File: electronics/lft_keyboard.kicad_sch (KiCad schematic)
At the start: 61 parts, among them J3 Conn_01x05_Female, J4 Conn_01x05_Male, SW1 SW_SPST, SW10 SW_SPST, SW11 SW_SPST, SW12 SW_SPST, SW13 SW_SPST, SW14 SW_SPST, SW15 SW_SPST, SW16 SW_SPST, SW17 SW_SPST, SW18 SW_SPST, SW19 SW_SPST, SW2 SW_SPST, SW20 SW_SPST, SW21 SW_SPST, SW22 SW_SPST, SW23 SW_SPST, SW24 SW_SPST, SW25 SW_SPST, SW26 SW_SPST, SW27 SW_SPST, SW28 SW_SPST, SW29 SW_SPST, SW3 SW_SPST, SW4 SW_SPST, SW5 SW_SPST, SW6 SW_SPST, SW7 SW_SPST, SW8 SW_SPST, SW9 SW_SPST, U2 PCA9675PW

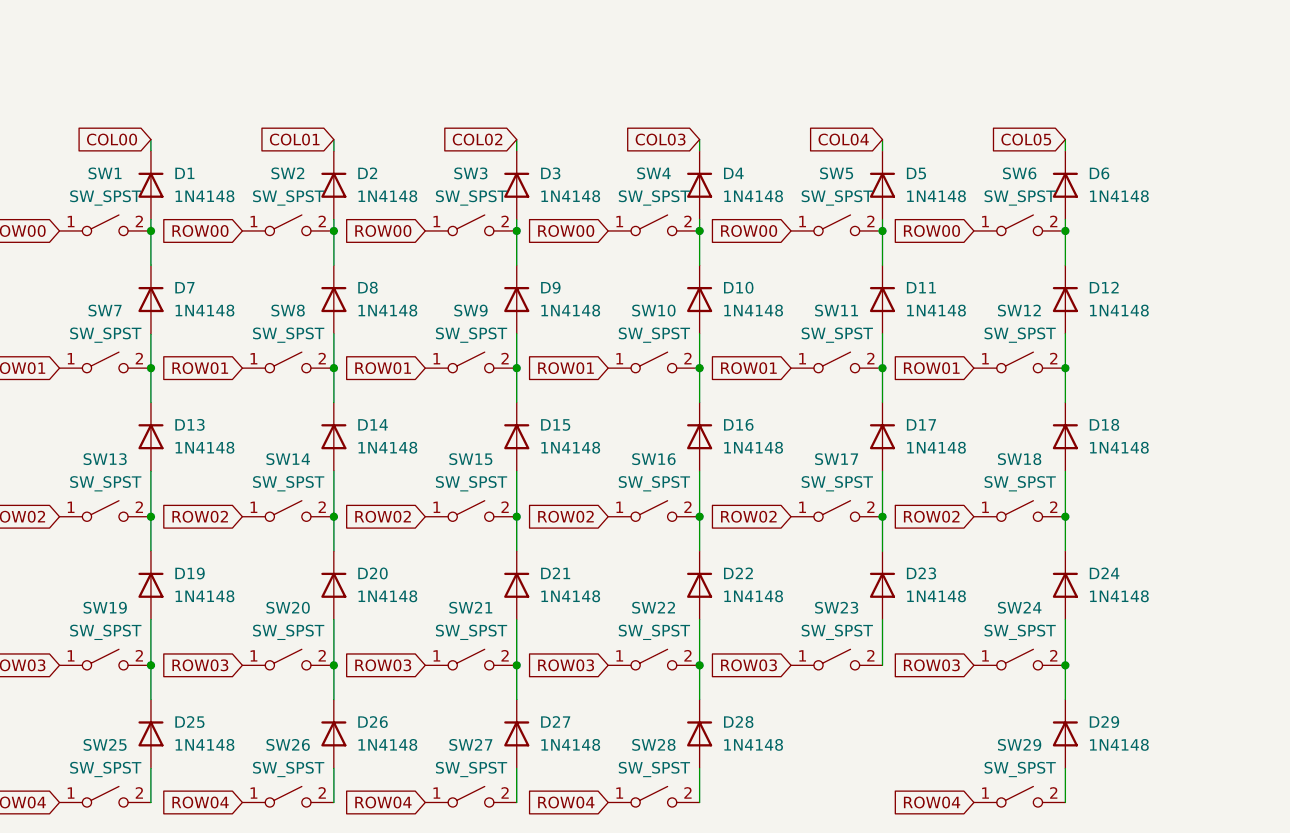
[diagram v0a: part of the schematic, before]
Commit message: update diode libraries
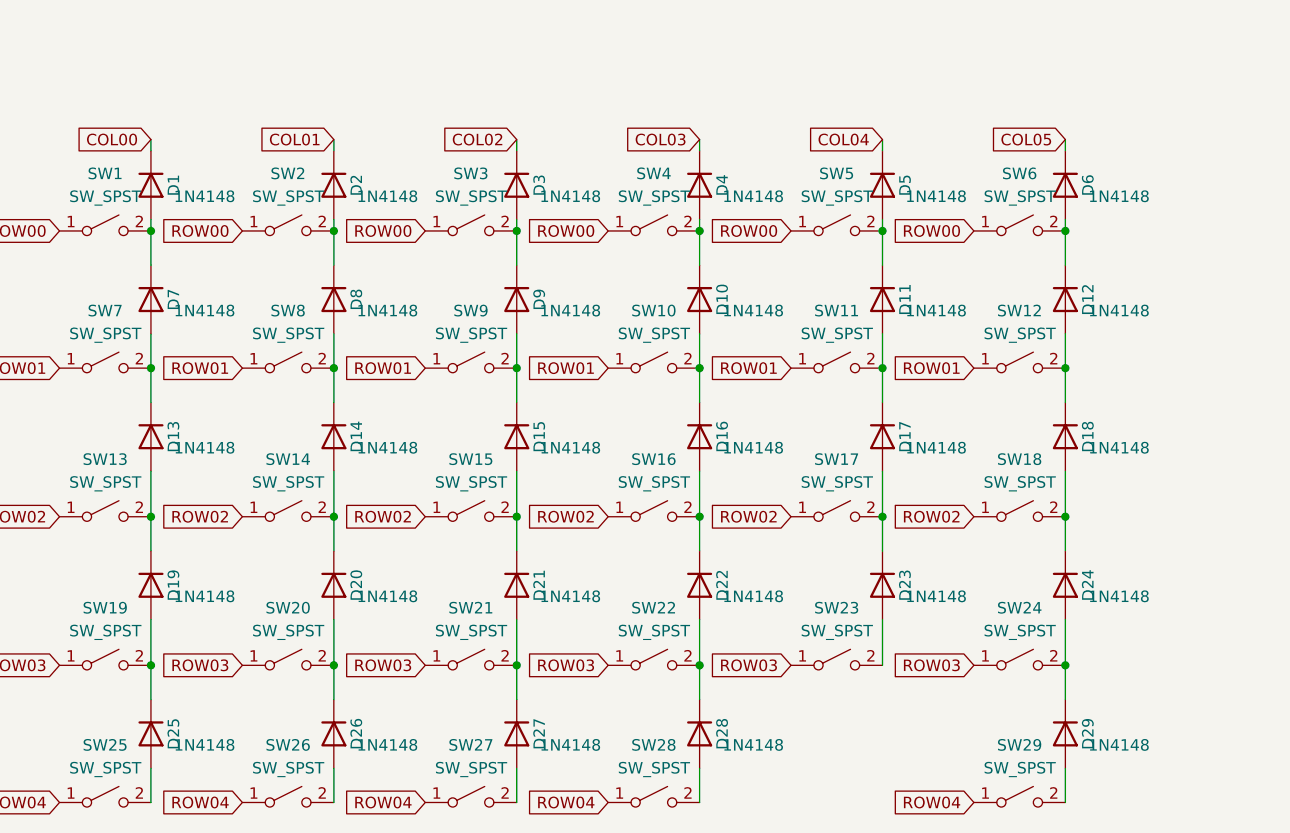
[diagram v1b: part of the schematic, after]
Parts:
- D1, D10, D11, D12, D13, D14, D15, D16, D17, D18, D19, D2, D20, D21, D22, D23, D24, D25, D26, D27, D28, D29, D3, D4, D5, D6, D7, D8, D9: footprint Diode_SMD:D_SOD-123 -> Diode_THT:D_DO-35_SOD27_P7.62mm_Horizontal; symbol Diode:1N4148W -> 1N4148:1N4148

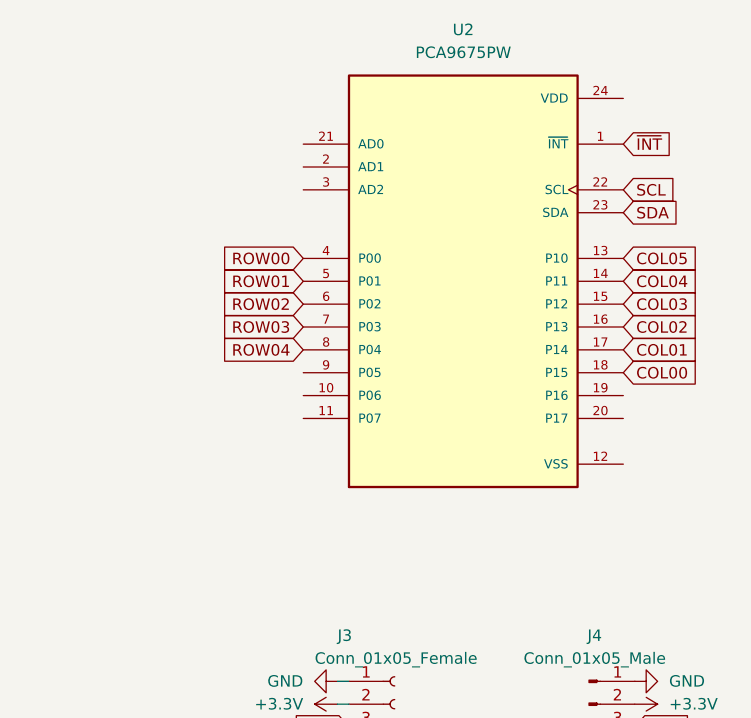
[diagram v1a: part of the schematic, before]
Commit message: add power and i2c addressing
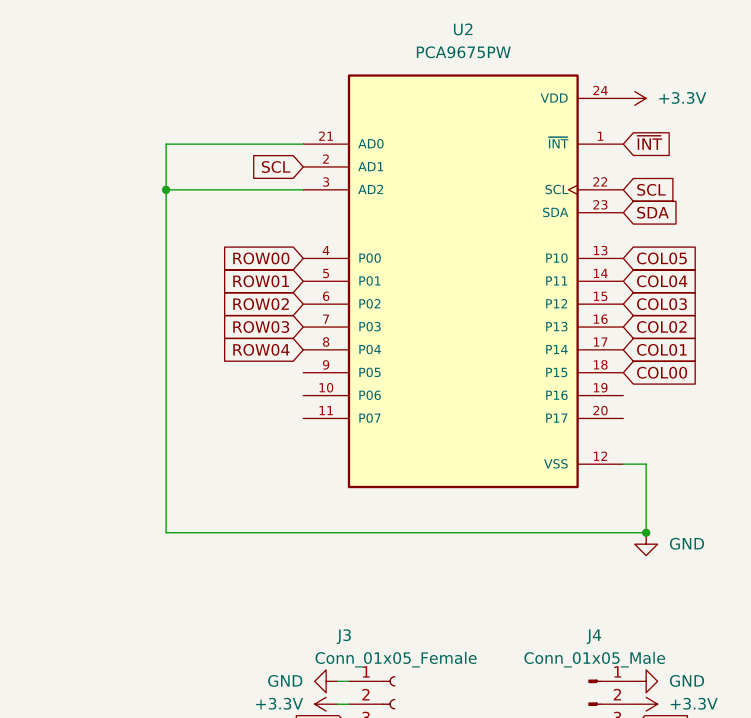
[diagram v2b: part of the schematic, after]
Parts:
- D1, D10, D11, D12, D13, D14, D15, D16, D17, D18, D19, D2, D20, D21, D22, D23, D24, D25, D26, D27, D28, D29, D3, D4, D5, D6, D7, D8, D9: footprint Diode_THT:D_DO-35_SOD27_P7.62mm_Horizontal -> 1N4148:1N4148
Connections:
- net +3V3: now also U2.24 (VDD)
- net GND: now also U2.12 (VSS), U2.21 (AD0), U2.3 (AD2)
- net SCL: now also U2.2 (AD1)
